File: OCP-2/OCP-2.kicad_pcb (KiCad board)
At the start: 2 copper layers, 100 x 100 mm, 140 parts, among them X1 ico*отверстие*М3, X2 ico*отверстие*М3

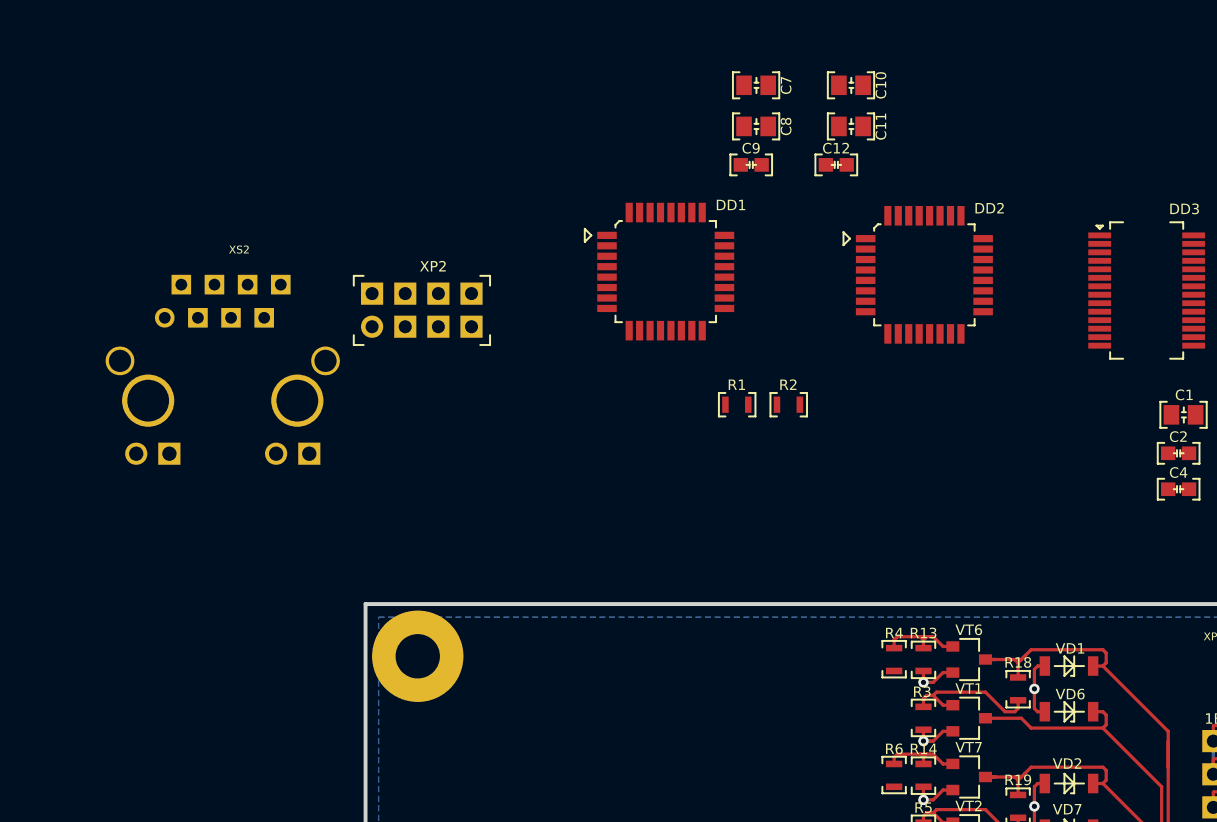
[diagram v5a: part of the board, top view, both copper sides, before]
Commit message: схема подключения ETH без SPI и светодиодов
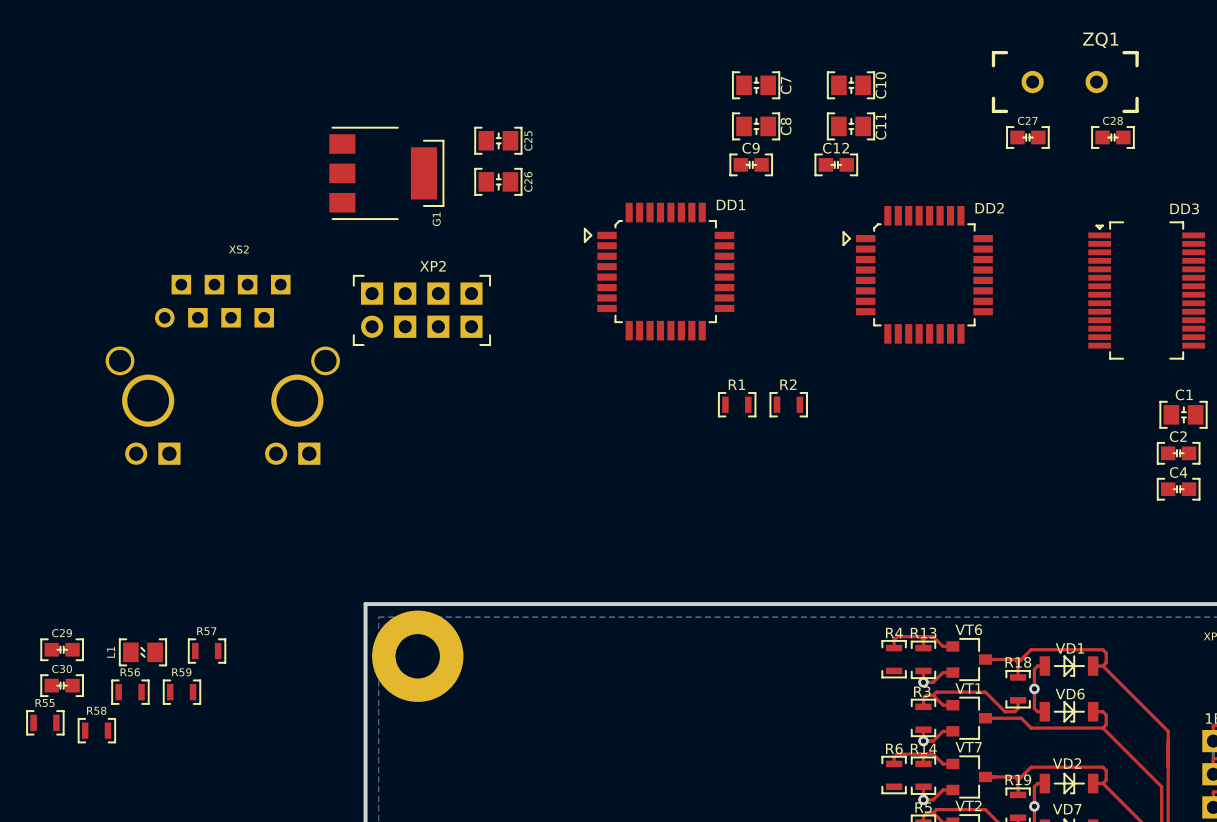
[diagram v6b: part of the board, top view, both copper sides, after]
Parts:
- added C25: Конденсатор*10мкФ*16В*0805, N_RLC:Конденсатор_SMD_IEC_0805, F.Cu at (59.2, 14.5)
- added C26: Конденсатор*10мкФ*16В*0805, N_RLC:Конденсатор_SMD_IEC_0805, F.Cu at (59.2, 17.6)
- added C27: Конденсатор*12пФ*50В*0603, N_RLC:Конденсатор_SMD_IEC_0603, F.Cu at (100.8, 14.2)
- added C28: Конденсатор*12пФ*50В*0603, N_RLC:Конденсатор_SMD_IEC_0603, F.Cu at (107.3, 14.2)
- added C29: Конденсатор*0,1мкФ*25В*0603, N_RLC:Конденсатор_SMD_IEC_0603, F.Cu at (26.8, 53.5)
- added C30: Конденсатор*0,1мкФ*25В*0603, N_RLC:Конденсатор_SMD_IEC_0603, F.Cu at (26.8, 56.2)
- added G1: LDO*вход_18Вmax*выход_3,3В*ток_1,2АSOT-223, N_VD_HL:Транзистор_NPN_SOT223_pnp, F.Cu at (51.4, 17.0)
- added L1: Чип-индуктивность*0,56мкГн*150мА*0805, N_RLC:Резистор_SMD_IEC_0805_0,125_Вт, F.Cu at (32.0, 53.7)
- added R55: Резистор*49,9кОм*0603, N_RLC:Резистор_SMD_0603_0,065_Вт_pnp, F.Cu at (25.4, 59.1)
- added R56: Резистор*49,9кОм*0603, N_RLC:Резистор_SMD_0603_0,065_Вт_pnp, F.Cu at (32.0, 56.8)
- added R57: Резистор*49,9кОм*0603, N_RLC:Резистор_SMD_0603_0,065_Вт_pnp, F.Cu at (37.8, 53.6)
- added R58: Резистор*49,9кОм*0603, N_RLC:Резистор_SMD_0603_0,065_Вт_pnp, F.Cu at (29.4, 59.7)
- added R59: Резистор*2,32кОм*0603, N_RLC:Резистор_SMD_0603_0,065_Вт_pnp, F.Cu at (35.9, 56.8)
- added ZQ1: Резонатор*25МГц*HC-49U, N_RLC:Резонатор_РК456МДУ(DIP), F.Cu at (101.1, 10.0)
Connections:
- DD3 pad 12: Net-(DD3-Pad12) -> /TPIN-
- DD3 pad 13: Net-(DD3-Pad13) -> /TPIN+
- DD3 pad 14: Net-(DD3-Pad14) -> /RBIAS
- DD3 pad 16: Net-(DD3-Pad16) -> /TPOUT-
- DD3 pad 17: Net-(DD3-Pad17) -> /TPOUT+
- DD3 pad 23: Net-(DD3-Pad23) -> /OSC1
- DD3 pad 24: Net-(DD3-Pad24) -> /OSC2
- XP1 pad 1B: Net-(XP1-Pad1B) -> 5V
- XP2 pad 1B: Net-(XP2-Pad1B) -> 5V
- XS2 pad 1: Net-(XS2-Pad1) -> /TPOUT+
- XS2 pad 2: Net-(XS2-Pad2) -> /TPOUT-
- XS2 pad 3: Net-(XS2-Pad3) -> /TPIN+
- XS2 pad 4: Net-(XS2-Pad4) -> /MID-TX
- XS2 pad 6: Net-(XS2-Pad6) -> /TPIN-
- XS2 pad 8: Net-(XS2-Pad8) -> GND

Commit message: полная схема подключен ETH и МК, нет клеммников
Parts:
- added R60: Резистор*1кОм*0603, N_RLC:Резистор_SMD_0603_0,065_Вт_pnp, F.Cu at (32.8, 16.5)
- added R61: Резистор*1кОм*0603, N_RLC:Резистор_SMD_0603_0,065_Вт_pnp, F.Cu at (32.8, 19.4)
- added R62: Резистор*10кОм*0603, N_RLC:Резистор_SMD_0603_0,065_Вт_pnp, F.Cu at (36.7, 16.5)
- added R63: Резистор*10кОм*0603, N_RLC:Резистор_SMD_0603_0,065_Вт_pnp, F.Cu at (36.7, 19.4)
- added R64: Резистор*1кОм*0603, N_RLC:Резистор_SMD_0603_0,065_Вт_pnp, F.Cu at (40.6, 16.5)
- added R65: Резистор*1кОм*0603, N_RLC:Резистор_SMD_0603_0,065_Вт_pnp, F.Cu at (40.6, 19.4)
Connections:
- net /MISO.M renamed /ETH.MISO
- net /MOSI.M renamed /ETH.MOSI
- DD1 pad 1: Net-(DD1-Pad1) -> /MC.DIN1
- DD1 pad 10: Net-(DD1-Pad10) -> /MC.DIN4
- DD1 pad 11: Net-(DD1-Pad11) -> /MC.DIN5
- DD1 pad 12: Net-(DD1-Pad12) -> /MC.DIN6
- DD1 pad 13: Net-(DD1-Pad13) -> /ETH.RES
- DD1 pad 14: Net-(DD1-Pad14) -> /ETH.CS
- DD1 pad 17: /SCK.M -> /ETH.CLK
- DD1 pad 2: Net-(DD1-Pad2) -> /MC.DIN2
- DD1 pad 23: Net-(DD1-Pad23) -> /MC.OUT1
- DD1 pad 24: Net-(DD1-Pad24) -> /MC.OUT2
- DD1 pad 25: Net-(DD1-Pad25) -> /MC.OUT3
- DD1 pad 26: Net-(DD1-Pad26) -> /MC.OUT4
- DD1 pad 27: Net-(DD1-Pad27) -> /SDA
- DD1 pad 28: Net-(DD1-Pad28) -> /SCL
- DD1 pad 32: Net-(DD1-Pad32) -> /ETH.INT
- DD1 pad 9: Net-(DD1-Pad9) -> /MC.DIN3
- DD2 pad 10: Net-(DD2-Pad10) -> /MC.DIN8
- DD2 pad 11: Net-(DD2-Pad11) -> /MC.DIN9
- DD2 pad 12: Net-(DD2-Pad12) -> /MC.DIN10
- DD2 pad 13: Net-(DD2-Pad13) -> /MC.DIN11
- DD2 pad 14: Net-(DD2-Pad14) -> /MC.DIN12
- DD2 pad 23: Net-(DD2-Pad23) -> /MC.OUT5
- DD2 pad 24: Net-(DD2-Pad24) -> /MC.OUT6
- DD2 pad 25: Net-(DD2-Pad25) -> /MC.OUT7
- DD2 pad 26: Net-(DD2-Pad26) -> /MC.OUT8
- DD2 pad 27: Net-(DD2-Pad27) -> /SDA
- DD2 pad 28: Net-(DD2-Pad28) -> /SCL
- DD2 pad 30: Net-(DD2-Pad30) -> /MC.OUT9
- DD2 pad 31: Net-(DD2-Pad31) -> /MC.OUT10
- DD2 pad 9: Net-(DD2-Pad9) -> /MC.DIN7
- DD3 pad 10: Net-(DD3-Pad10) -> /ETH.RES
- DD3 pad 26: Net-(DD3-Pad26) -> /LEDB
- DD3 pad 27: Net-(DD3-Pad27) -> /LEDA
- DD3 pad 4: Net-(DD3-Pad4) -> /ETH.INT
- DD3 pad 8: Net-(DD3-Pad8) -> /ETH.CLK
- DD3 pad 9: Net-(DD3-Pad9) -> /ETH.CS
- XP2 pad 2A: /SCK.M -> /ETH.CLK
- XS2 pad 11: Net-(XS2-Pad11) -> /LEDB
- XS2 pad 8: GND -> Net-(XS2-Pad8)
- XS2 pad 9: Net-(XS2-Pad9) -> /LEDA

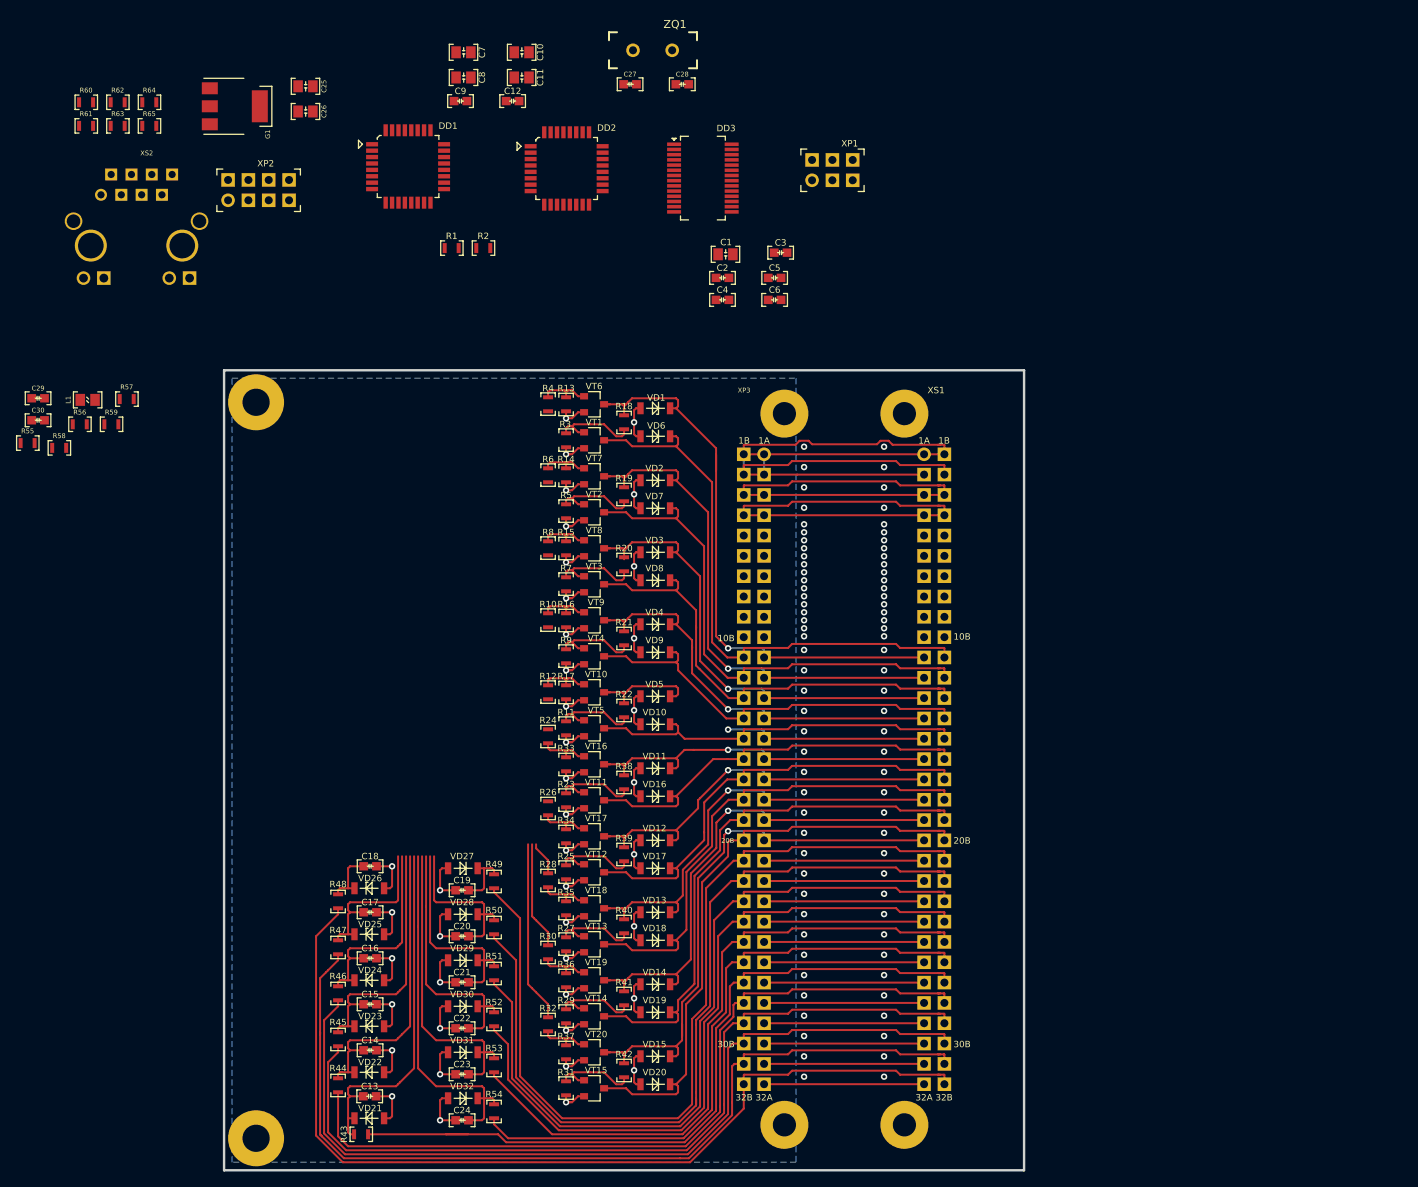
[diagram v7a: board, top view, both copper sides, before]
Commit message: схема включения ETH + клеммники вместо СНП306
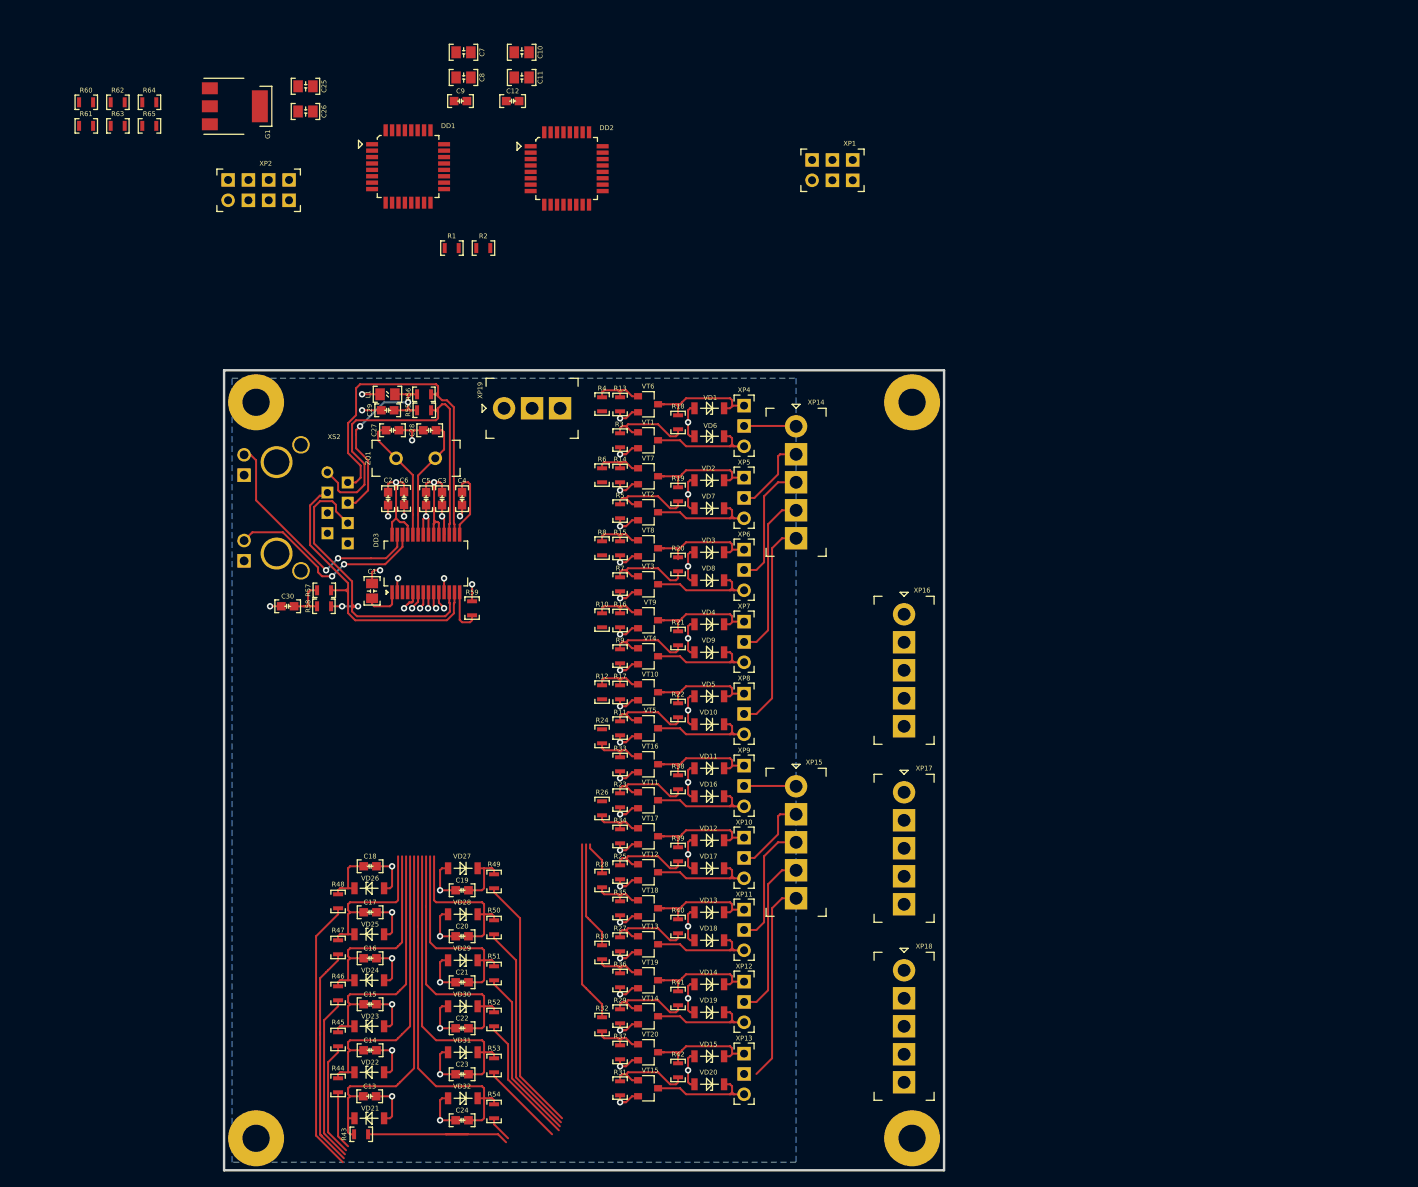
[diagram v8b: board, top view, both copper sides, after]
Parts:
- removed XP3: Вилка*DIN41612R*64контакта*2ряда*угловая, MOTOR_X:Вилка_СНП306-64ВП21-24-1
- removed XS1: Розетка*DIN41612R*64контакта*2ряда*угловая, MOTOR_X:Розетка_СНП306-64РП21_угловая
- added X3: ico*отверстие*М3, N_X:Отверстие_М3, F.Cu at (136.0, 54.0)
- added X4: ico*отверстие*М3, N_X:Отверстие_М3, F.Cu at (136.0, 146.0)
- added XP10: Вилка*PLS*3контактов*1ряд*вертикальная, N_X:Вилка_PLS3_вертикальная, F.Cu at (115.0, 113.5)
- added XP11: Вилка*PLS*3контактов*1ряд*вертикальная, N_X:Вилка_PLS3_вертикальная, F.Cu at (115.0, 122.5)
- added XP12: Вилка*PLS*3контактов*1ряд*вертикальная, N_X:Вилка_PLS3_вертикальная, F.Cu at (115.0, 131.5)
- added XP13: Вилка*PLS*3контактов*1ряд*вертикальная, N_X:Вилка_PLS3_вертикальная, F.Cu at (115.0, 140.5)
- added XP14: Клеммник*шаг_3,5*5контактов*1ряд*вертикальная, N_X:Клеммник_15EDGVC-3.5-05P, F.Cu at (121.5, 57.0)
- added XP15: Клеммник*шаг_3,5*5контактов*1ряд*вертикальная, N_X:Клеммник_15EDGVC-3.5-05P, F.Cu at (121.5, 102.0)
- added XP16: Клеммник*шаг_3,5*5контактов*1ряд*вертикальная, N_X:Клеммник_15EDGVC-3.5-05P, F.Cu at (135.0, 80.5)
- added XP17: Клеммник*шаг_3,5*5контактов*1ряд*вертикальная, N_X:Клеммник_15EDGVC-3.5-05P, F.Cu at (135.0, 102.8)
- added XP18: Клеммник*шаг_3,5*5контактов*1ряд*вертикальная, N_X:Клеммник_15EDGVC-3.5-05P, F.Cu at (135.0, 125.0)
- added XP19: Клеммник*шаг_3,5*3контактов*1ряд*вертикальная, N_X:Клеммник_15EDGVC-3.5-03P, F.Cu at (85.0, 54.8)
- added XP4: Вилка*PLS*3контактов*1ряд*вертикальная, N_X:Вилка_PLS3_вертикальная, F.Cu at (115.0, 59.5)
- added XP5: Вилка*PLS*3контактов*1ряд*вертикальная, N_X:Вилка_PLS3_вертикальная, F.Cu at (115.0, 68.5)
- added XP6: Вилка*PLS*3контактов*1ряд*вертикальная, N_X:Вилка_PLS3_вертикальная, F.Cu at (115.0, 77.5)
- added XP7: Вилка*PLS*3контактов*1ряд*вертикальная, N_X:Вилка_PLS3_вертикальная, F.Cu at (115.0, 86.5)
- added XP8: Вилка*PLS*3контактов*1ряд*вертикальная, N_X:Вилка_PLS3_вертикальная, F.Cu at (115.0, 95.5)
- added XP9: Вилка*PLS*3контактов*1ряд*вертикальная, N_X:Вилка_PLS3_вертикальная, F.Cu at (115.0, 104.5)
- moved DD3 66.2 mm to (71.0, 77.8), turned to 90 degrees
- moved C1 59.7 mm to (68.5, 76.7), turned to 270 degrees
- moved ZQ1 59.0 mm to (71.5, 61.0)
- moved C28 53.5 mm to (75.7, 57.5), turned to 180 degrees
- moved C6 52.5 mm to (72.5, 66.0), turned to 270 degrees
- moved C27 52.5 mm to (71.0, 57.5)
- moved C3 52.3 mm to (77.2, 66.0), turned to 270 degrees
- moved C5 51.6 mm to (75.2, 66.0), turned to 270 degrees
- moved R59 50.6 mm to (81.0, 79.8), turned to 90 degrees
- moved C2 50.1 mm to (70.5, 66.0), turned to 270 degrees
- moved R55 49.7 mm to (75.0, 55.0)
- moved XS2 44.8 mm to (62.9, 62.8), turned to 270 degrees
- moved C29 43.7 mm to (70.5, 55.0), turned to 180 degrees
- moved R56 43.2 mm to (75.0, 53.0), turned to 180 degrees
- moved C4 41.0 mm to (79.8, 66.0), turned to 270 degrees
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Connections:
- R59 pad 2: Net-(R59-Pad2) -> GND
- XS2 pad 8: Net-(XS2-Pad8) -> GND
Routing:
- net 5V: track 148.6 -> 39.4 mm
- net /DIN2: track 99.1 -> 7.27 mm
- net /DIN3: track 104.7 -> 14.4 mm
- net /DIN4: track 109.5 -> 21.1 mm
- net /DIN5: track 114.7 -> 28.2 mm
- net /DIN6: track 118.3 -> 34.3 mm
- net /DIN7: track 111.2 -> 32.3 mm
- net /DIN8: track 105.1 -> 27.0 mm
- net /DIN12: track 79.2 -> 3.22 mm
- net /DIN9: track 97.0 -> 21.7 mm
- net GND: track 255.6 -> 180.4 mm, vias 32 -> 44
- net /DIN1: track 94.6 -> 20.4 mm
- net /DIN10: track 89.9 -> 16.4 mm
- net /DIN11: track 83.2 -> 10.8 mm
- net /DOUT10.PNP: track 74.6 -> 13.6 mm
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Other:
- board size 100 x 100 mm -> 90 x 100 mm
